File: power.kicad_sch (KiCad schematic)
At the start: 89 parts, among them J6 Molex_Nano-Fit_1x2_105309-2202, Q1 BSS138-7-F, Q2 SI7613DN-T1-GE3, Q3 BSS138-7-F, Q4 SSM3J332R, U18 TPS56C230, U19 TPS56C230, U20 TPS3840PL30DBVR, U21 TPS564247DRLR, U22 TPS564247DRLR, U23 TLV73333PDBVT, U48 INA219AIDCNR, U49 INA219AIDCNR, U50 INA219AIDCNR

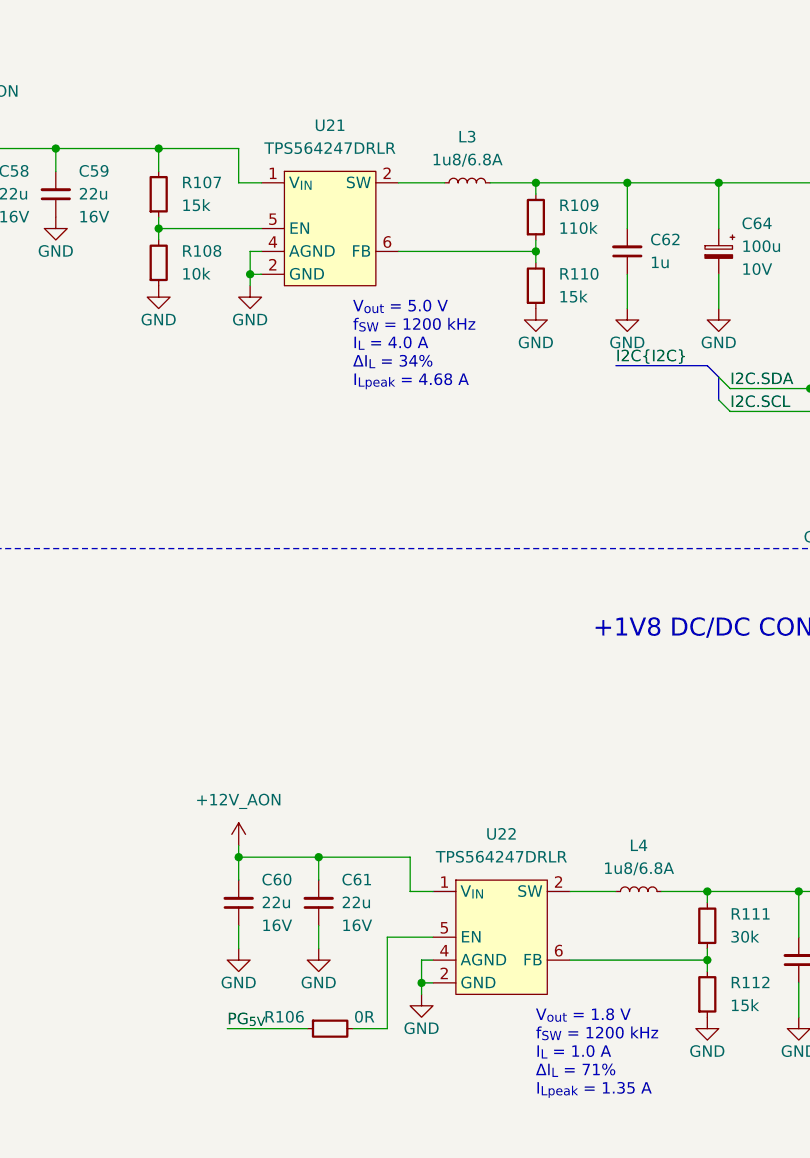
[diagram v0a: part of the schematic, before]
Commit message: [#58137] Update TPS564247DRLR symbol
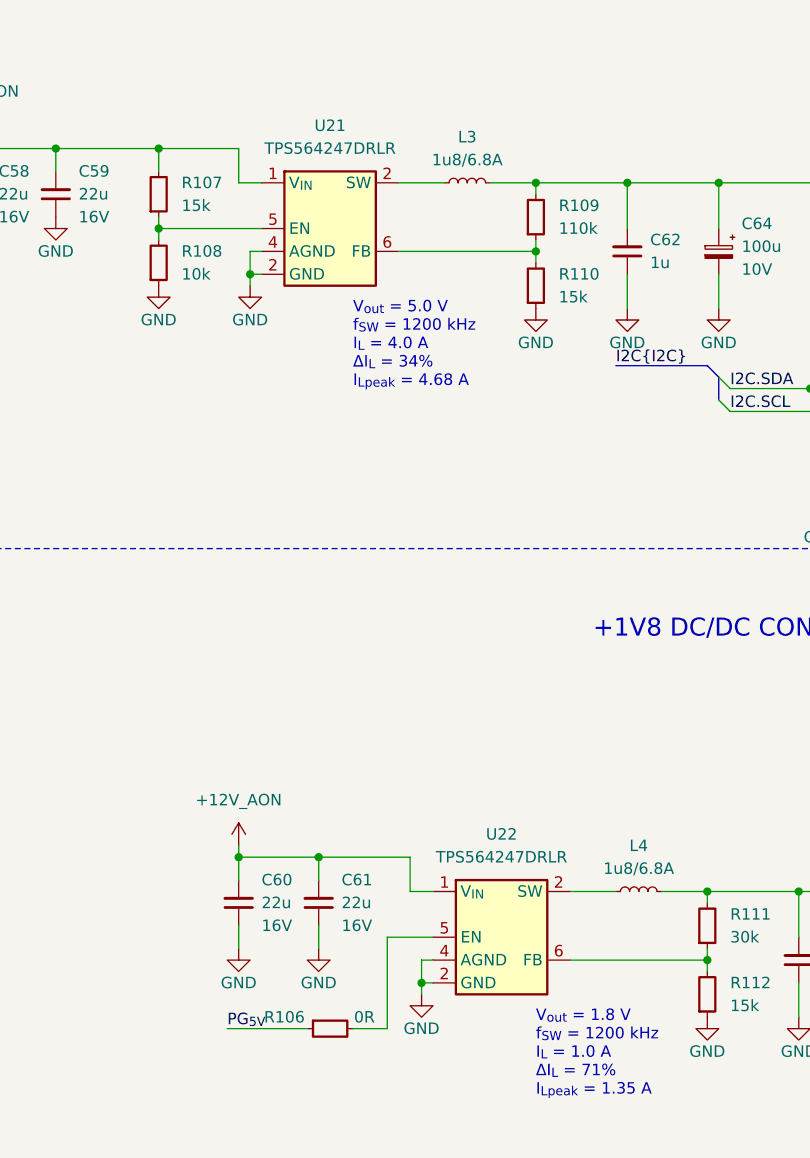
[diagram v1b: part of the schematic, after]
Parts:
- U21, U22: footprint (none) -> antmicro-footprints:SOT-563; Author (none) -> Antmicro; License (none) -> Apache-2.0
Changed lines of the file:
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@@
     )
   )
-  (symbol (lib_id "antmicroDCDCConverters:TPS564247DRLR") (at 281.94 132.08 0) (unit 1)
+  (symbol (lib_id "antmicroDCDCConverters:TPS564247DRLR") (at 279.4 134.62 0) (unit 1)
     (in_bom yes) (on_board yes) (dnp no) (fields_autoplaced)
     (property "Reference" "U22" (at 287.02 128.27 0)
       (effects (font (size 1.27 1.27)))
     )
-    (property "Value" "TPS564247DRLR" (at 281.94 132.08 0)
+    (property "Value" "TPS564247DRLR" (at 279.4 134.62 0)
       (effects (font (size 1.27 1.27)) hide)
     )
-    (property "Footprint" "" (at 281.94 132.08 0)
+    (property "Footprint" "antmicro-footprints:SOT-563" (at 279.4 134.62 0)
       (effects (font (size 1.27 1.27)) hide)
     )
-    (property "Datasheet" "https://www.ti.com/lit/ds/symlink/tps564247.pdf?ts=1713526387938&ref_url=https%253A%252F%252Fwww.mouser.pl%252F" (at 281.94 132.08 0)
+    (property "Datasheet" "https://www.ti.com/lit/ds/symlink/tps564247.pdf?ts=1713526387938&ref_url=https%253A%252F%252Fwww.mouser.pl%252F" (at 279.4 134.62 0)
       (effects (font (size 1.27 1.27)) hide)
     )
-    (property "Manufcaturer" "Texas Instruments" (at 281.94 132.08 0)
+    (property "Manufcaturer" "Texas Instruments" (at 279.4 134.62 0)
       (effects (font (size 1.27 1.27)) hide)
     )
@@
       (effects (font (size 1.27 1.27)))
     )
+    (property "Author" "Antmicro" (at 309.88 154.94 0)
+      (effects (font (size 1.27 1.27) (thickness 0.15)) (justify left bottom) hide)
+    )
+    (property "License" "Apache-2.0" (at 309.88 157.48 0)
+      (effects (font (size 1.27 1.27) (thickness 0.15)) (justify left bottom) hide)
+    )
     (pin "1")
     (pin "6")
@@
     )
   )
+  (symbol (lib_id "antmicroDCDCConverters:TPS564247DRLR") (at 260.35 55.88 0) (unit 1)
+    (in_bom yes) (on_board yes) (dnp no) (fields_autoplaced)
+    (property "Reference" "U21" (at 267.97 49.53 0)
+      (effects (font (size 1.27 1.27)))
+    )
+    (property "Value" "TPS564247DRLR" (at 260.35 55.88 0)
+      (effects (font (size 1.27 1.27)) hide)
+    )
+    (property "Footprint" "antmicro-footprints:SOT-563" (at 260.35 55.88 0)
+      (effects (font (size 1.27 1.27)) hide)
+    )
+    (property "Datasheet" "https://www.ti.com/lit/ds/symlink/tps564247.pdf?ts=1713526387938&ref_url=https%253A%252F%252Fwww.mouser.pl%252F" (at 260.35 55.88 0)
+      (effects (font (size 1.27 1.27)) hide)
+    )
+    (property "Manufcaturer" "Texas Instruments" (at 260.35 55.88 0)
+      (effects (font (size 1.27 1.27)) hide)
+    )
+    (property "MPN" "TPS564247DRLR" (at 267.97 52.07 0)
+      (effects (font (size 1.27 1.27)))
+    )
+    (property "Author" "Antmicro" (at 290.83 76.2 0)
+      (effects (font (size 1.27 1.27) (thickness 0.15)) (justify left bottom) hide)
+    )
+    (property "License" "Apache-2.0" (at 290.83 78.74 0)
+      (effects (font (size 1.27 1.27) (thickness 0.15)) (justify left bottom) hide)
+    )
+    (pin "1")
+    (pin "6")
+    (pin "2")
+    (pin "2")
+    (pin "5")
+    (pin "4")
+    (instances
+      (project "com-express-7-baseboard"
+        (path "/1b8c34da-dad5-4b0b-8c4b-45db766c4dfa/9e43a8fe-5590-4346-856e-e8b6e5166965"
+          (reference "U21") (unit 1)
+        )
+      )
+    )
+  )
   (symbol (lib_id "antmicroCapacitors0402:C_100n_0402") (at 185.42 162.56 90) (unit 1)
     (in_bom yes) (on_board yes) (dnp no) (fields_autoplaced)
@@
         )
       )
-    )
-  )
-  (symbol (lib_id "antmicroDCDCConverters:TPS564247DRLR") (at 262.89 53.34 0) (unit 1)
-    (in_bom yes) (on_board yes) (dnp no) (fields_autoplaced)
-    (property "Reference" "U21" (at 267.97 49.53 0)
-      (effects (font (size 1.27 1.27)))
-    )
-    (property "Value" "TPS564247DRLR" (at 262.89 53.34 0)
-      (effects (font (size 1.27 1.27)) hide)
-    )
-    (property "Footprint" "" (at 262.89 53.34 0)
-      (effects (font (size 1.27 1.27)) hide)
-    )
-    (property "Datasheet" "https://www.ti.com/lit/ds/symlink/tps564247.pdf?ts=1713526387938&ref_url=https%253A%252F%252Fwww.mouser.pl%252F" (at 262.89 53.34 0)
-      (effects (font (size 1.27 1.27)) hide)
-    )
-    (property "Manufcaturer" "Texas Instruments" (at 262.89 53.34 0)
-      (effects (font (size 1.27 1.27)) hide)
-    )
-    (property "MPN" "TPS564247DRLR" (at 267.97 52.07 0)
-      (effects (font (size 1.27 1.27)))
-    )
-    (pin "1")
-    (pin "6")
-    (pin "2")
-    (pin "2")
-    (pin "5")
-    (pin "4")
-    (instances
-      (project "com-express-7-baseboard"
-        (path "/1b8c34da-dad5-4b0b-8c4b-45db766c4dfa/9e43a8fe-5590-4346-856e-e8b6e5166965"
-          (reference "U21") (unit 1)
-        )
-      )

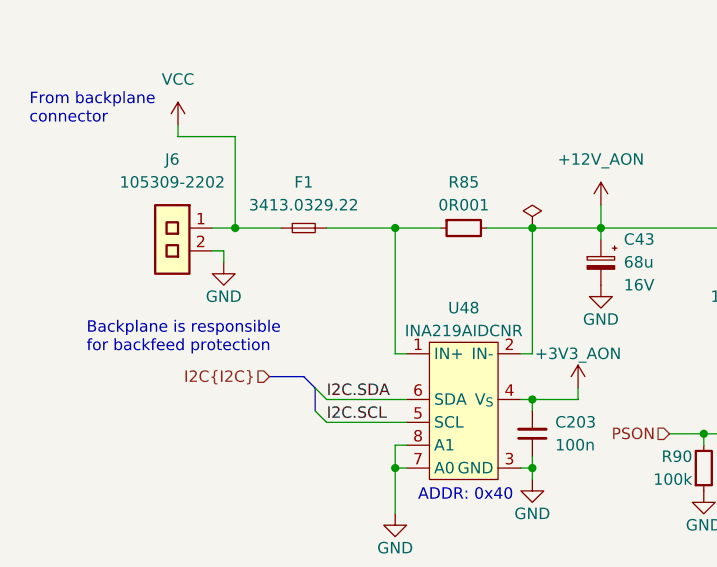
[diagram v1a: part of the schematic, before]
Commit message: [#58137] Add input voltage and buttons ESD protection
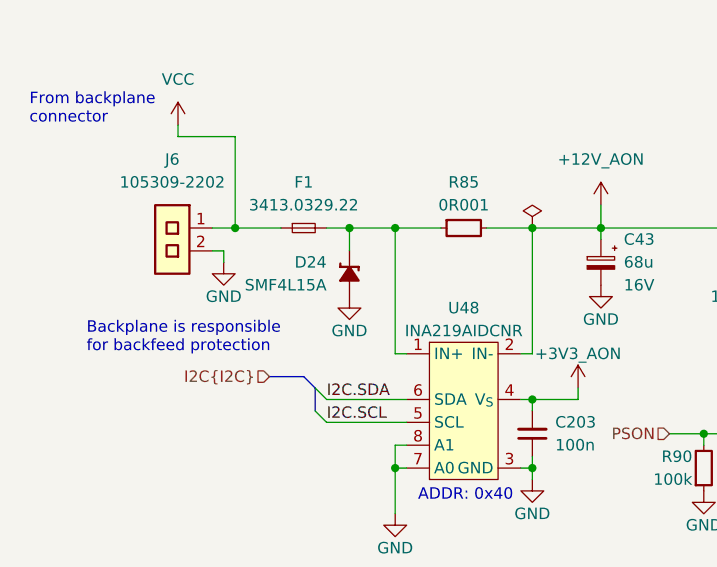
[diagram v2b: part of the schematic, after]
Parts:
- added D24: SMF4L15A, antmicro-footprints:SOD-123FL, symbol antmicroTVSDiodes:SMF4L15A
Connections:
- net GND: now also D24.2 (A)
- net at F1.2, R85.1, U48.1 (IN+): now also D24.1 (C)
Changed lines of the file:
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@@
   (junction (at 322.58 55.88) (diameter 0) (color 0 0 0 0)
   )
+  (junction (at 49.53 224.79) (diameter 0) (color 0 0 0 0)
+  )
   (junction (at 237.49 52.07) (diameter 0) (color 0 0 0 0)
   )
@@
     (stroke (width 0) (type default))
   )
+  (wire (pts (xy 49.53 224.79) (xy 49.53 227.33))
+    (stroke (width 0) (type default))
+  )
   (wire (pts (xy 259.08 63.5) (xy 259.08 66.04))
     (stroke (width 0) (type default))
@@
     (stroke (width 0) (type default))
   )
+  (wire (pts (xy 49.53 224.79) (xy 54.61 224.79))
+    (stroke (width 0) (type default))
+  )
   (wire (pts (xy 228.6 52.07) (xy 228.6 54.61))
     (stroke (width 0) (type default))
@@
     (stroke (width 0) (type default))
   )
-  (wire (pts (xy 46.99 224.79) (xy 54.61 224.79))
+  (wire (pts (xy 46.99 224.79) (xy 49.53 224.79))
     (stroke (width 0) (type default))
   )
@@
     )
   )
+  (symbol (lib_id "antmicropower:GND") (at 49.53 232.41 0) (mirror y) (unit 1)
+    (in_bom yes) (on_board yes) (dnp no)
+    (property "Reference" "#PWR0447" (at 40.64 234.95 0)
+      (effects (font (size 1.27 1.27) (thickness 0.15)) (justify left bottom) hide)
+    )
+    (property "Value" "GND" (at 49.53 236.22 0)
+      (effects (font (size 1.27 1.27) (thickness 0.15)))
+    )
+    (property "Footprint" "" (at 40.64 240.03 0)
+      (effects (font (size 1.27 1.27) (thickness 0.15)) (justify left bottom) hide)
+    )
+    (property "Datasheet" "" (at 40.64 245.11 0)
+      (effects (font (size 1.27 1.27) (thickness 0.15)) (justify left bottom) hide)
+    )
+    (property "Author" "Antmicro" (at 40.64 240.03 0)
+      (effects (font (size 1.27 1.27) (thickness 0.15)) (justify left bottom) hide)
+    )
+    (property "License" "Apache-2.0" (at 40.64 242.57 0)
+      (effects (font (size 1.27 1.27) (thickness 0.15)) (justify left bottom) hide)
+    )
+    (pin "1")
+    (instances
+      (project "com-express-7-baseboard"
+        (path "/1b8c34da-dad5-4b0b-8c4b-45db766c4dfa/9e43a8fe-5590-4346-856e-e8b6e5166965"
+          (reference "#PWR0447") (unit 1)
+        )
+      )
+    )
+  )
   (symbol (lib_id "antmicroCapacitors0603:C_22u_16V_0603") (at 228.6 59.69 90) (unit 1)
     (in_bom yes) (on_board yes) (dnp no) (fields_autoplaced)
@@
         )
       )
+    )
+  )
+  (symbol (lib_id "antmicroTVSDiodes:SMF4L15A") (at 49.53 227.33 90) (mirror x) (unit 1)
+    (in_bom yes) (on_board yes) (dnp no) (fields_autoplaced)
+    (property "Reference" "D24" (at 46.99 228.5999 90)
+      (effects (font (size 1.27 1.27) (thickness 0.15)) (justify left))
+    )
+    (property "Value" "SMF4L15A" (at 64.77 254 0)
+      (effects (font (size 1.27 1.27) (thickness 0.15)) (justify left bottom) hide)
+    )
+    (property "Footprint" "antmicro-footprints:SOD-123FL" (at 59.69 254 0)
+      (effects (font (size 1.27 1.27) (thickness 0.15)) (justify left bottom) hide)
+    )
+    (property "Datasheet" "https://www.littelfuse.com/media?resourcetype=datasheets&itemid=d2ba8fab-1de3-4176-8530-f36ecb0b8799&filename=smf4l" (at 62.23 254 0)
+      (effects (font (size 1.27 1.27) (thickness 0.15)) (justify left bottom) hide)
+    )
+    (property "MPN" "SMF4L15A" (at 46.99 231.1399 90)
+      (effects (font (size 1.27 1.27) (thickness 0.15)) (justify left))
+    )
+    (property "Manufacturer" "Littelfuse" (at 67.31 254 0)
+      (effects (font (size 1.27 1.27) (thickness 0.15)) (justify left bottom) hide)
+    )
+    (property "Author" "Antmicro" (at 69.85 254 0)
+      (effects (font (size 1.27 1.27) (thickness 0.15)) (justify left bottom) hide)
+    )
+    (property "License" "Apache-2.0" (at 72.39 254 0)
+      (effects (font (size 1.27 1.27) (thickness 0.15)) (justify left bottom) hide)
+    )
+    (pin "1")
+    (pin "2")
+    (instances
+      (project "com-express-7-baseboard"
+        (path "/1b8c34da-dad5-4b0b-8c4b-45db766c4dfa/9e43a8fe-5590-4346-856e-e8b6e5166965"
+          (reference "D24") (unit 1)
+        )
+      )

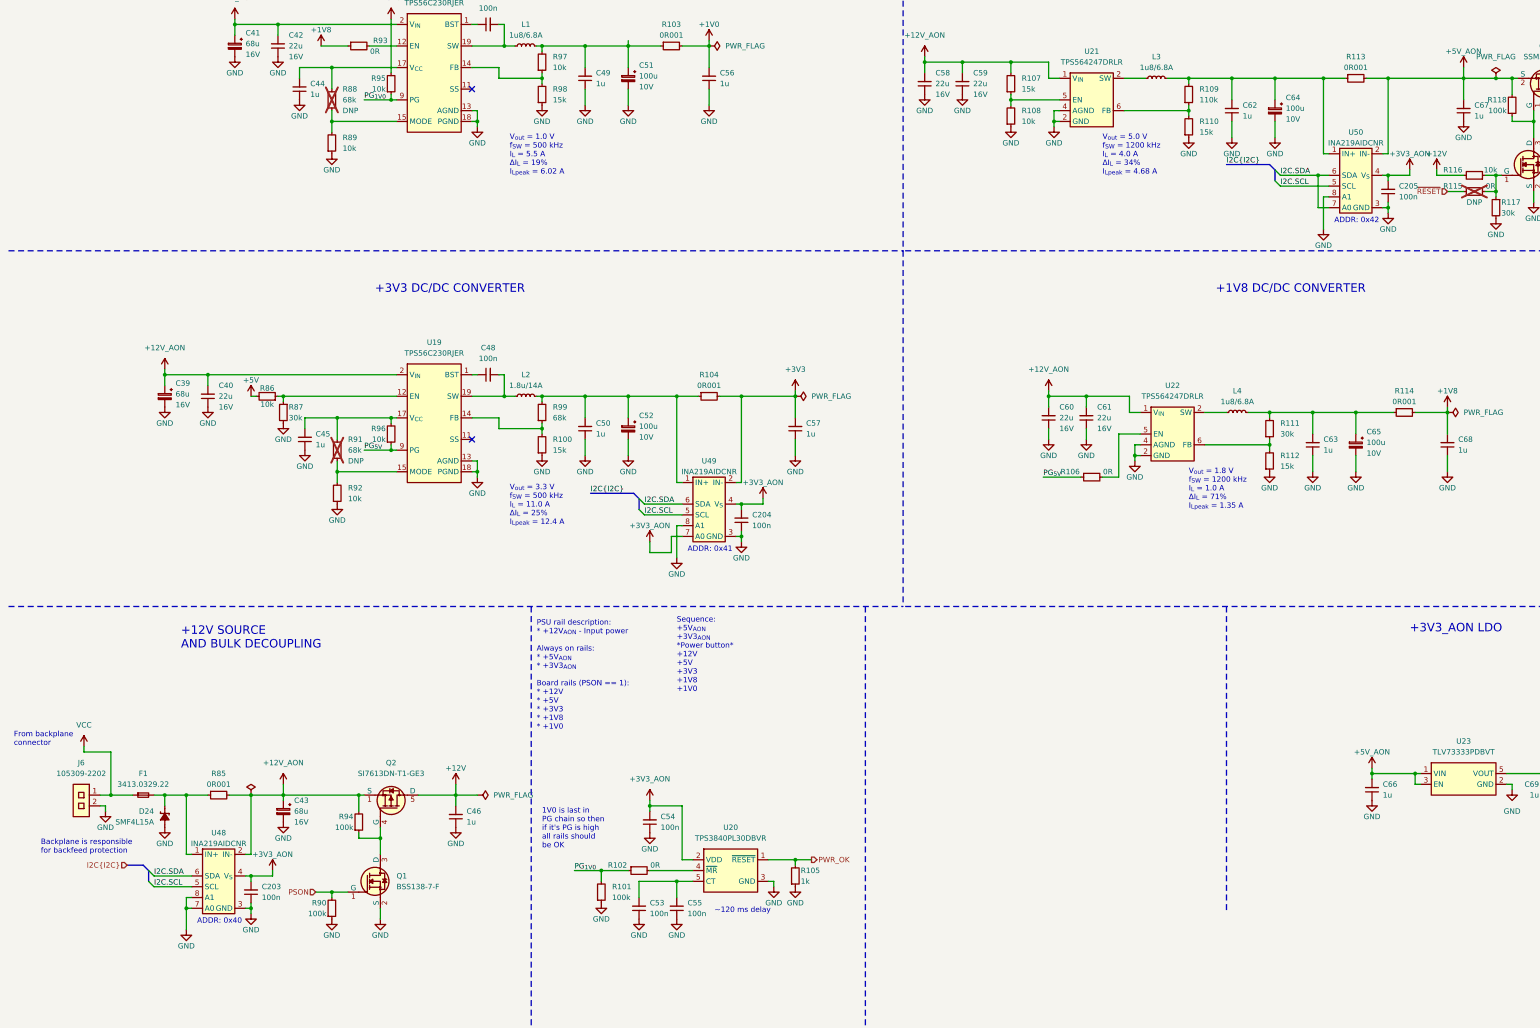
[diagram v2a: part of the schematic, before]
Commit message: [#58571] Mock initial placement
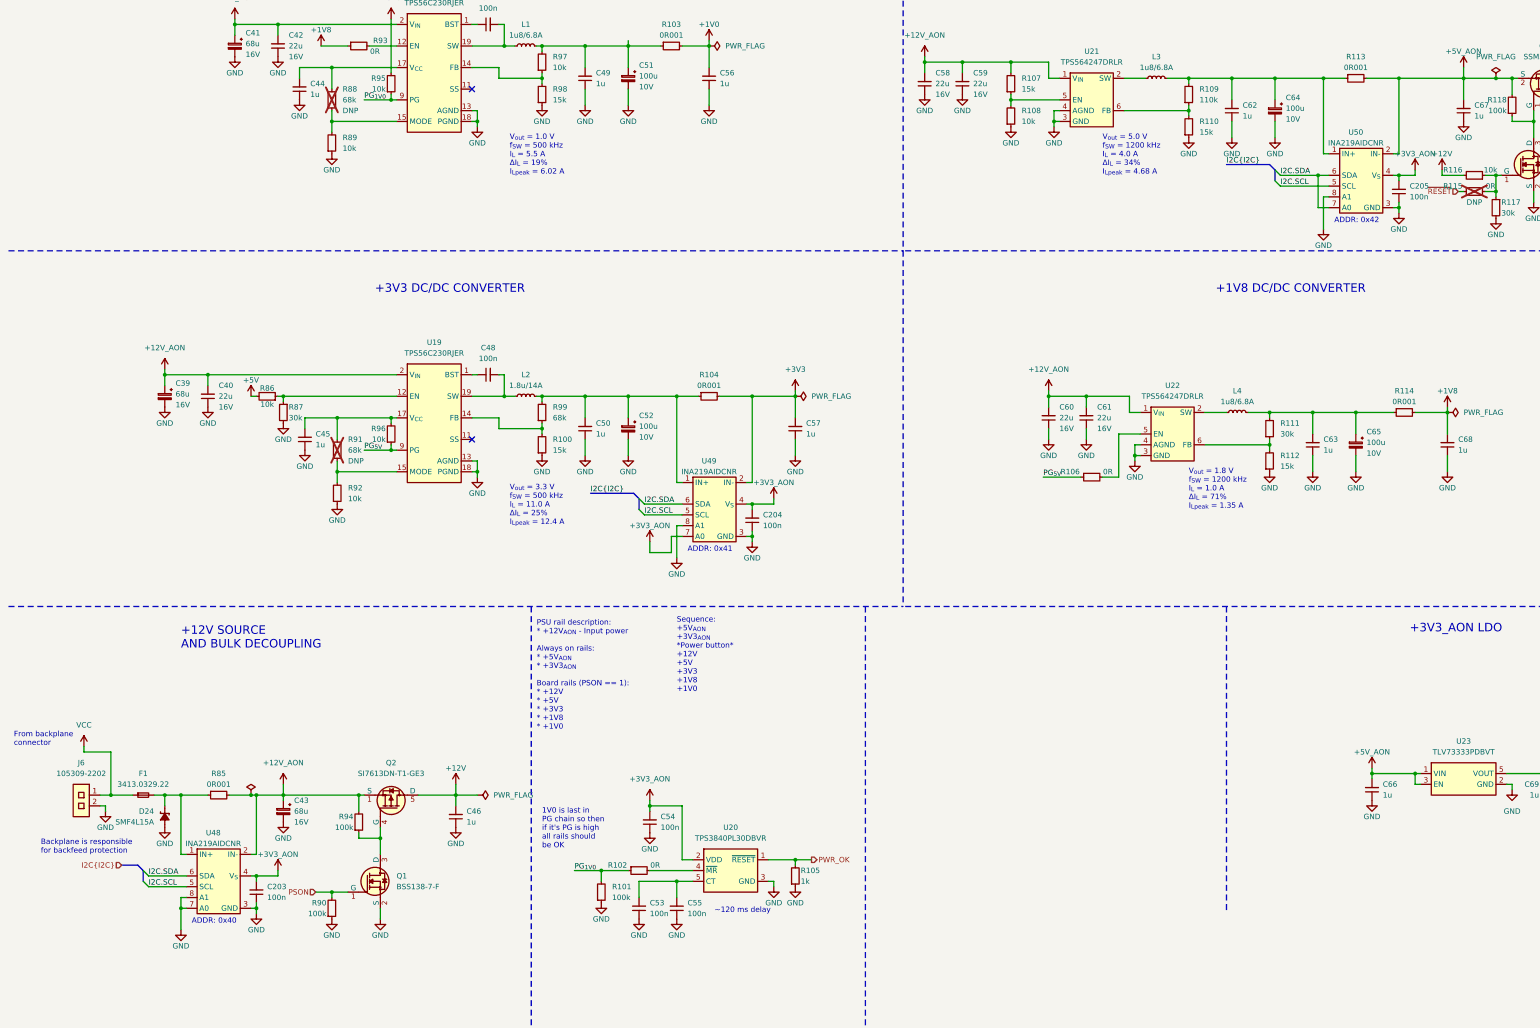
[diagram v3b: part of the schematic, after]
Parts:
- U21, U22: Manufacturer (none) -> Texas Instruments
- U48, U49, U50: footprint (none) -> antmicro-footprints:SOT-23-8; Author (none) -> Antmicro; License (none) -> Apache-2.0
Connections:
- net GND: now also U21.3 (GND), U22.3 (GND); no longer U21.2 (SW), U22.2 (SW)
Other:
- moved on the sheet: C203, C204, C205, U49, U50
